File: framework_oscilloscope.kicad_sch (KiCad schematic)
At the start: 83 parts, among them IC1 FT232HL-REEL, IC10 93LC56BT-I_OT, IC2 ICE40UP5K-SG48I, IC3 ADC08060CIMTX_NOPB, IC7 OPA356AIDBVR, IC8 TLV77312PDBVR, IC9 LM4040C20IDBZT, J1 BNC, P1 USB_C_Plug_USB2.0, U9 TPS62A02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

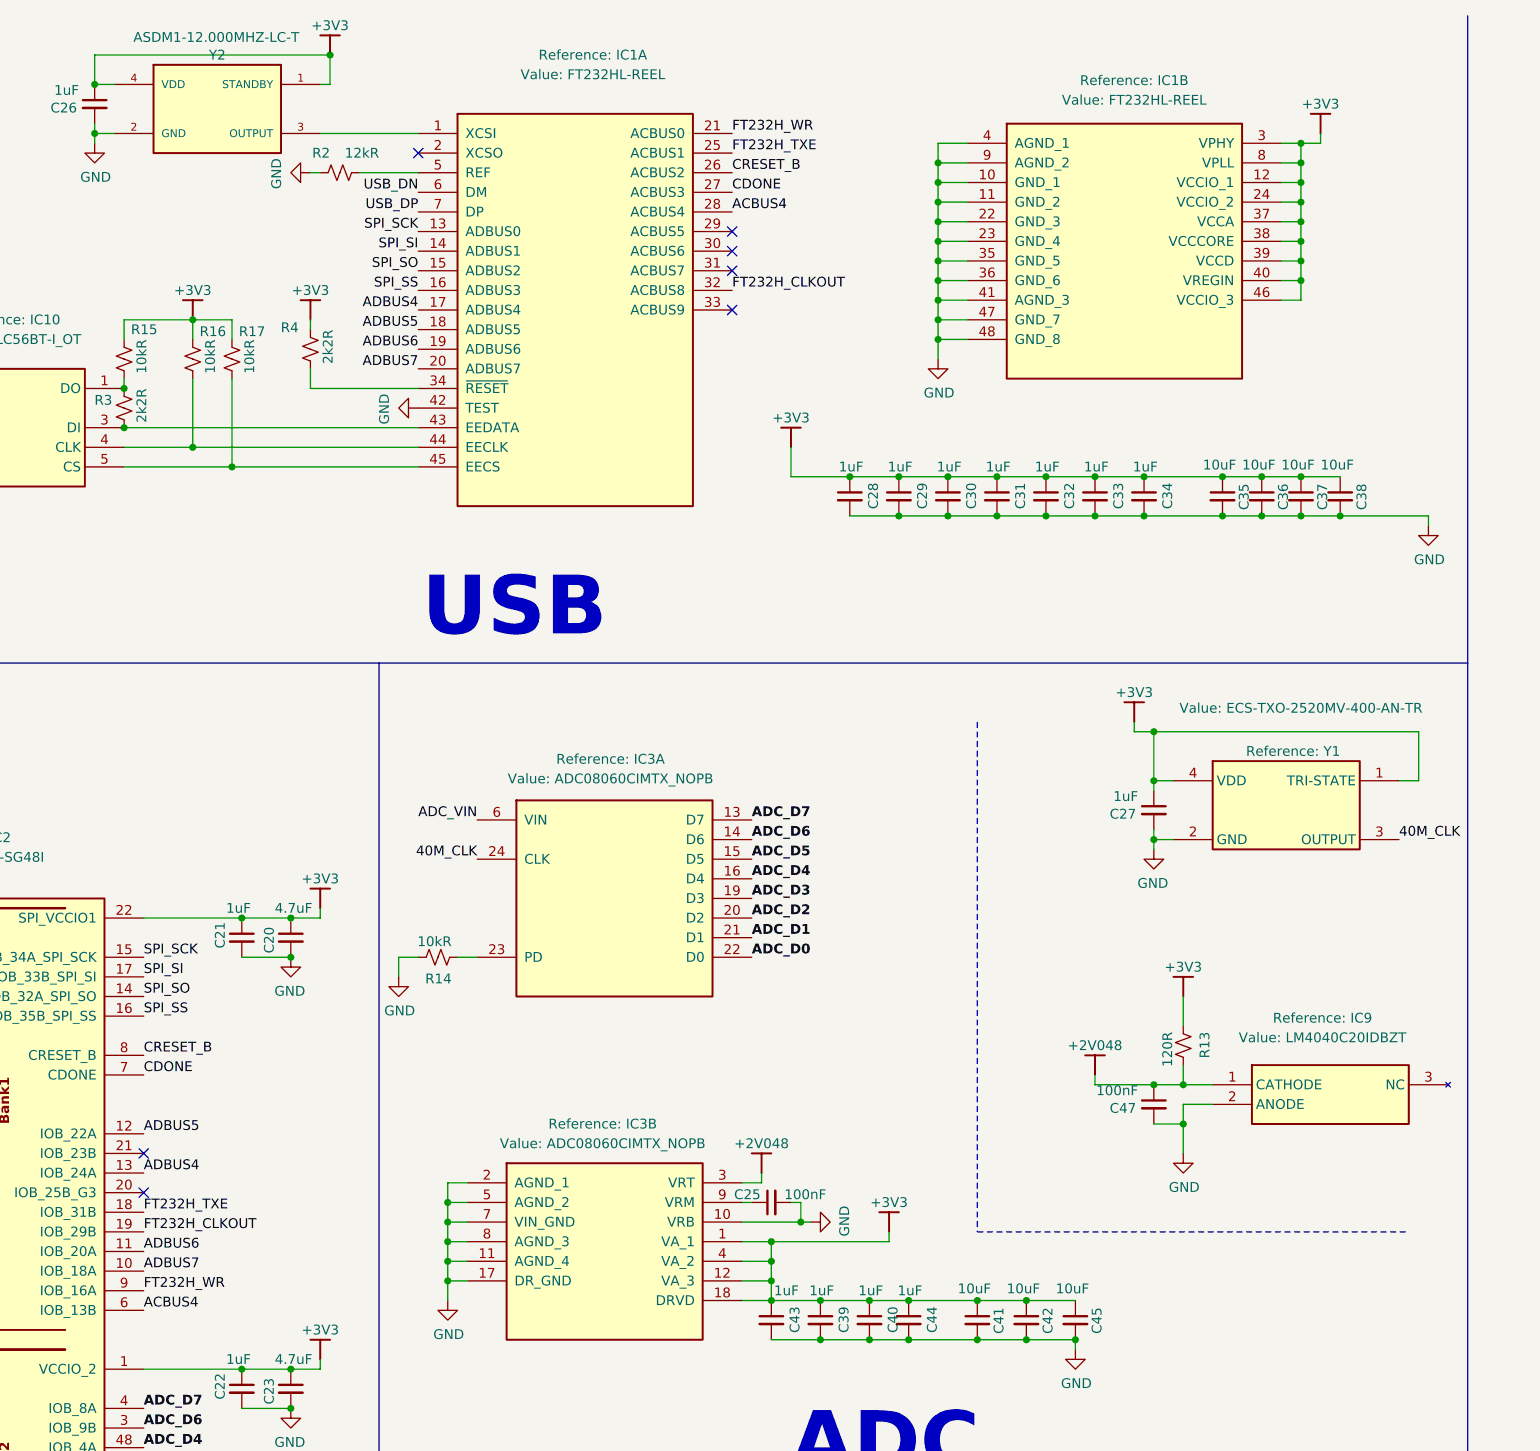
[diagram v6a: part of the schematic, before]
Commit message: fixed FT232-FPGA connections
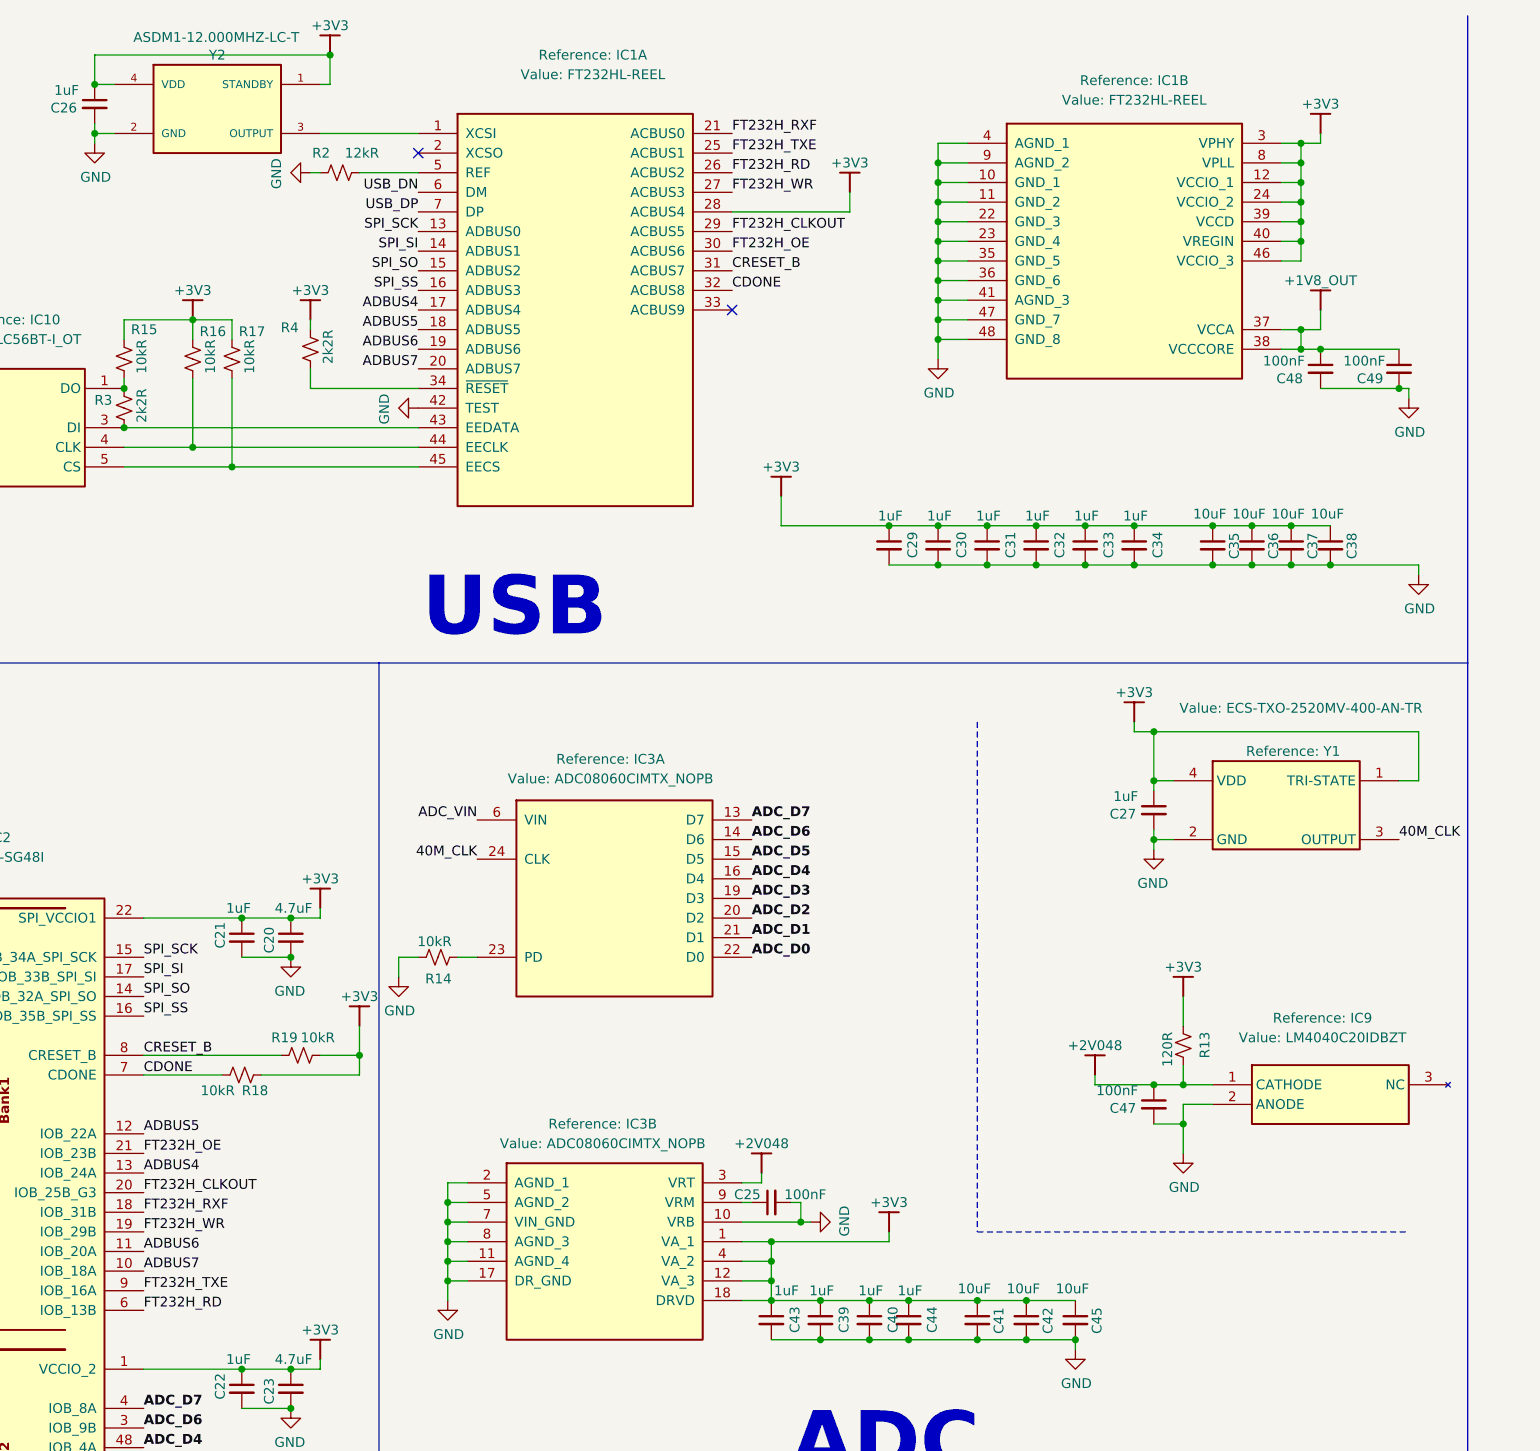
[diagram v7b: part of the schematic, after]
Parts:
- removed C28: 1uF, framework_oscilloscope:0402_1005Metric_CAP, symbol framework_oscilloscope:C_Small
- added C48, C49: 100nF, framework_oscilloscope:0402_1005Metric_CAP, symbol framework_oscilloscope:C_Small
- added R18, R19: 10kR, framework_oscilloscope:0402_1005Metric, symbol framework_oscilloscope:R_Small_US
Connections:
- net +3V3: now also IC1.28 (ACBUS4), R18.1, R19.1; no longer IC1.37 (VCCA), IC1.38 (VCCCORE)
- net CDONE: now also IC1.32 (ACBUS8), R18.2; no longer IC1.27 (ACBUS3)
- net CRESET_B: now also IC1.31 (ACBUS7), R19.2; no longer IC1.26 (ACBUS2)
- net FT232H_CLKOUT: now also IC1.29 (ACBUS5), IC2.20 (IOB_25B_G3); no longer IC1.32 (ACBUS8), IC2.19 (IOB_29B)
- net FT232H_TXE: now also IC2.9 (IOB_16A); no longer IC2.18 (IOB_31B)
- net FT232H_WR: now also IC1.27 (ACBUS3), IC2.19 (IOB_29B); no longer IC1.21 (ACBUS0), IC2.9 (IOB_16A)
- net GND: now also C48.2, C49.2
- net FT232H_OE: now reaches IC1.30 (ACBUS6)
- net FT232H_OE: now also IC2.21 (IOB_23B)
- net ACBUS4 renamed FT232H_RD
- net FT232H_RD: now also IC1.26 (ACBUS2); no longer IC1.28 (ACBUS4)
- new net +1V8_OUT: C48.1, C49.1, IC1.37 (VCCA), IC1.38 (VCCCORE)
- new net FT232H_RXF: IC1.21 (ACBUS0), IC2.18 (IOB_31B)
- no-connect marks 25 -> 20
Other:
- moved on the sheet: C29, C30, C31, C32, C33, C34, C35, C36, C37, C38

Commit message: changed front end bandwidth limit
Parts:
- C24: value 10pF -> 220pF
- R12: value 33R -> 75R
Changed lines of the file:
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@@
 	)
 	(junction
+		(at 140.97 147.32)
+		(diameter 0)
+		(color 0 0 0 0)
+	)
+	(junction
 		(at 243.84 111.76)
 		(diameter 0)
@@
 	)
 	(junction
-		(at 140.97 147.32)
-		(diameter 0)
-		(color 0 0 0 0)
-	)
-	(junction
 		(at 243.84 229.87)
 		(diameter 0)
@@
 		)
 		(property "Value" "10kR"
-			(at 133.35 145.034 90)
+			(at 133.858 145.034 90)
 			(show_name no)
 			(do_not_autoplace no)
@@
 			)
 		)
-		(property "Value" "10pF"
+		(property "Value" "220pF"
 			(at 263.398 243.078 90)
 			(show_name no)
@@
 			)
 		)
-		(property "Value" "33R"
+		(property "Value" "75R"
 			(at 259.588 234.188 90)
 			(show_name no)
